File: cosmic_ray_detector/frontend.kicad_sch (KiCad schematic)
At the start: 15 parts

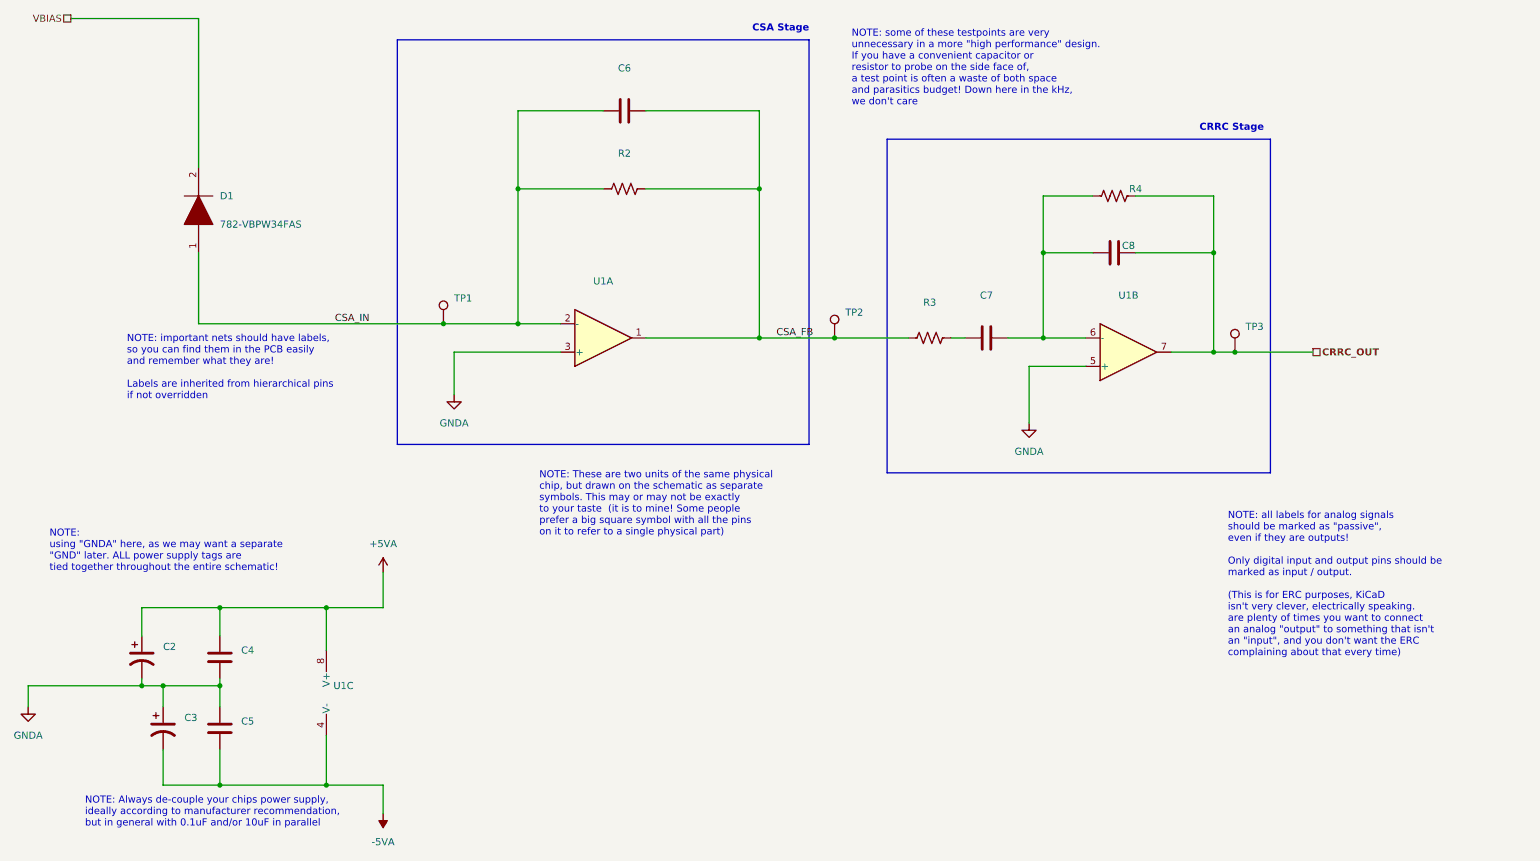
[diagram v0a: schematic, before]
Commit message: update routed / finished PCB to version 9
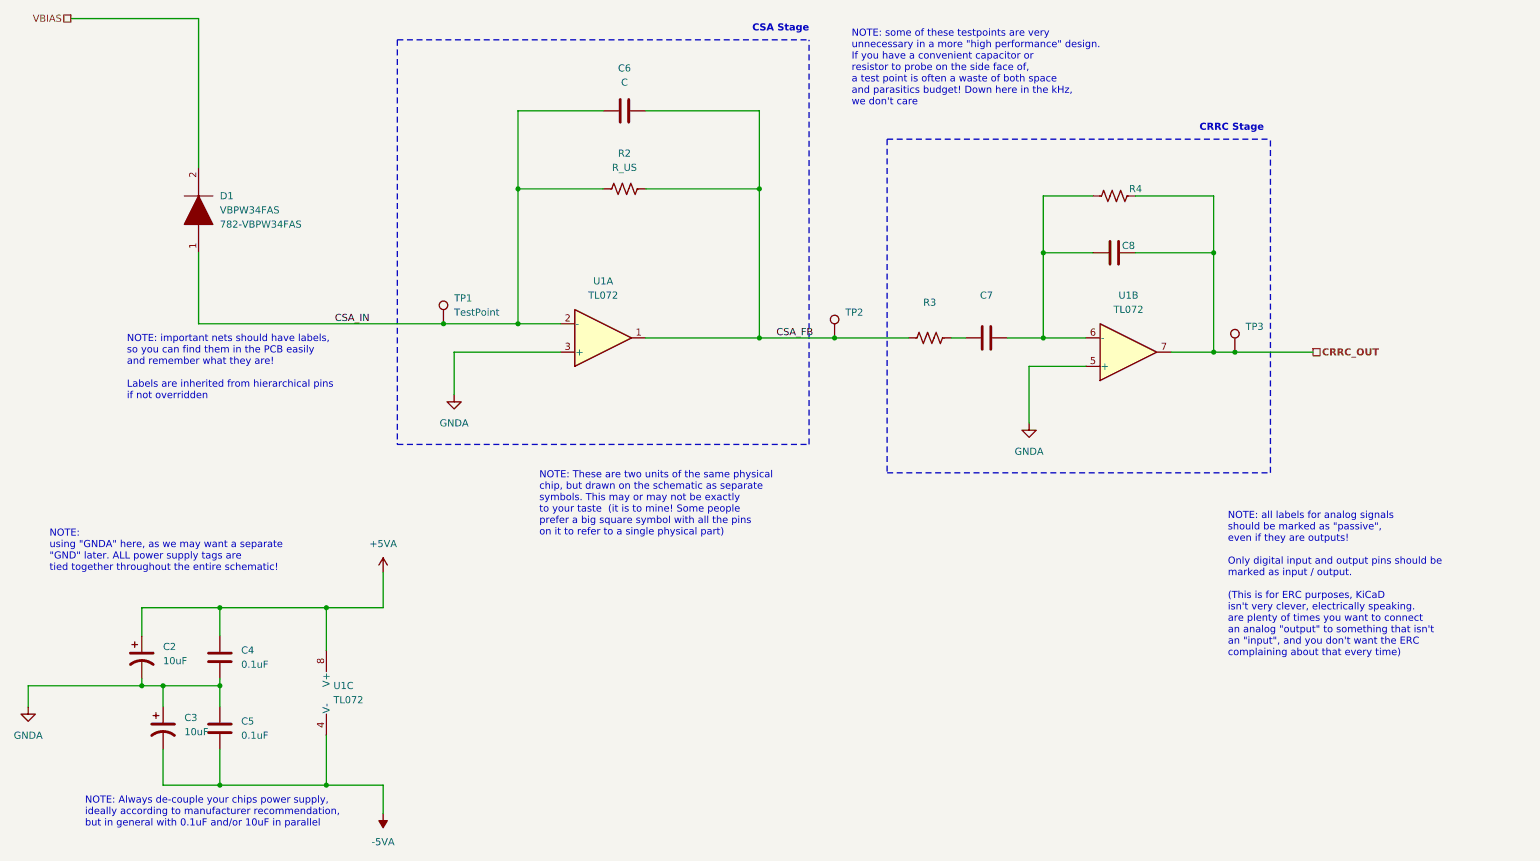
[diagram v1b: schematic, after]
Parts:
- C2, C3: value (none) -> 10uF; footprint (none) -> Capacitor_Tantalum_SMD:CP_EIA-3216-12_Kemet-S
- C4, C5: value (none) -> 0.1uF; footprint (none) -> Capacitor_SMD:C_0402_1005Metric
- C6: value (none) -> C; footprint (none) -> Capacitor_SMD:C_0402_1005Metric
- C7, C8: value (none) -> ~; footprint (none) -> Capacitor_SMD:C_0402_1005Metric
- D1: value (none) -> VBPW34FAS; footprint (none) -> cosmic_ray_detector_lib:VBPW34FAS
- R2: value (none) -> R_US; footprint (none) -> Resistor_SMD:R_0402_1005Metric
- R3, R4: value (none) -> ~; footprint (none) -> Resistor_SMD:R_0402_1005Metric
- TP1: value (none) -> TestPoint; footprint (none) -> cosmic_ray_detector_lib:harwin_tp_SMD
- TP2, TP3: value (none) -> ~; footprint (none) -> cosmic_ray_detector_lib:harwin_tp_SMD
- U1: value (none) -> TL072; footprint (none) -> Package_SO:SO-8_3.9x4.9mm_P1.27mm

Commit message: update pcb and schem to V10
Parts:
- C4, C5, C6: footprint Capacitor_SMD:C_0402_1005Metric -> cosmic_ray_detector_lib:C_0402_1005Metric
- C7, C8: value ~ -> (none); footprint Capacitor_SMD:C_0402_1005Metric -> cosmic_ray_detector_lib:C_0402_1005Metric
- R2: footprint Resistor_SMD:R_0402_1005Metric -> cosmic_ray_detector_lib:R_0402_1005Metric
- R3, R4: value ~ -> (none); footprint Resistor_SMD:R_0402_1005Metric -> cosmic_ray_detector_lib:R_0402_1005Metric
- TP2, TP3: value ~ -> (none)
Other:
- moved on the sheet: TP1, TP2
